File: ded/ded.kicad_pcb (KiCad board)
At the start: 2 copper layers, 10.6 x 15 mm, 2 parts, among them J1 USB_C_Receptacle_PowerOnly_6P, J2 USB_C_Receptacle_PowerOnly_6P

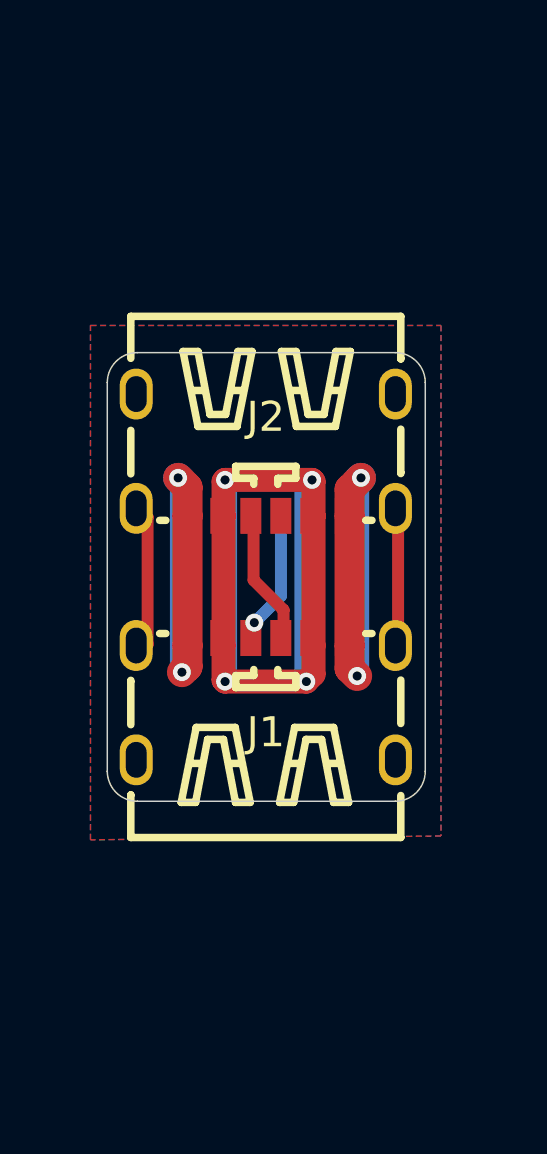
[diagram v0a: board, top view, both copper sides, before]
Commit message: add a hopefully-more-bendable spot to the usb coupler; fix drc; add sds
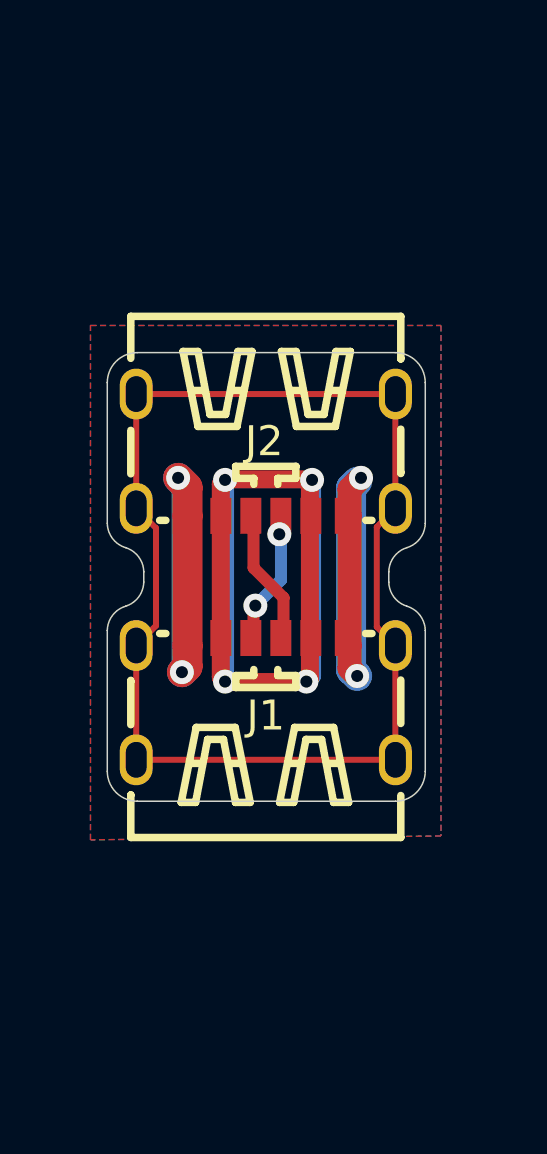
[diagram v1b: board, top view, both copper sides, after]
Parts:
- added G***: LOGO, ded:sds5050, B.Cu at (100.0, 101.1)
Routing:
- net /S1: track 0.00 -> 42.7 mm
- net (no net): track 9.88 -> 0.00 mm
- net Net-(J1-CC1): track 4.83 -> 4.75 mm, vias 1 -> 2
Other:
- outline, holes or cut-outs redrawn

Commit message: candidate designs for ded and deh couplers
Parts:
- removed J1, J2: USB_C_Receptacle_PowerOnly_6P, ded:TYPE-C-SMD_TYPE-C-6P_5
- added USB1: GT-USB-8016A, ded:USB-TYPE-C-SMD_GT-USB-8016A, F.Cu at (100.0, 106.3)
- added USB2: GT-USB-8016A, ded:USB-TYPE-C-SMD_GT-USB-8016A, F.Cu at (100.0, 95.9)
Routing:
- net /S1: track 42.7 -> 0.00 mm
- net VBUS: track 32.8 -> 9.93 mm, vias 4 -> 0
- net GND: track 26.9 -> 8.32 mm, vias 4 -> 3
- net Net-(USB1-TX1+): track 0.00 -> 13.2 mm, vias 0 -> 2
- net Net-(USB1-TX1-): track 0.00 -> 13.0 mm, vias 0 -> 2
- net Net-(USB1-RX1-): track 0.00 -> 12.0 mm, vias 0 -> 2
- net Net-(USB1-CC1): track 0.00 -> 11.2 mm, vias 0 -> 2
- net Net-(USB1-RX1+): track 0.00 -> 11.2 mm, vias 0 -> 2
- net Net-(USB1-D+): track 0.00 -> 10.0 mm, vias 0 -> 2
- net Net-(USB1-D-): track 0.00 -> 9.96 mm, vias 0 -> 2
- net (no net): track 0.00 -> 8.71 mm
- net Net-(J1-CC1): track 4.75 -> 0.00 mm, vias 2 -> 0
- net Net-(J1-CC2): track 4.74 -> 0.00 mm
- added copper zone on B.Cu, net GND
- added copper zone on F.Cu, net VBUS
- removed copper zone on F.Cu, net GND
- removed copper zone on B.Cu, net VBUS
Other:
- board size 10.6 x 15 mm -> 13 x 15.2 mm

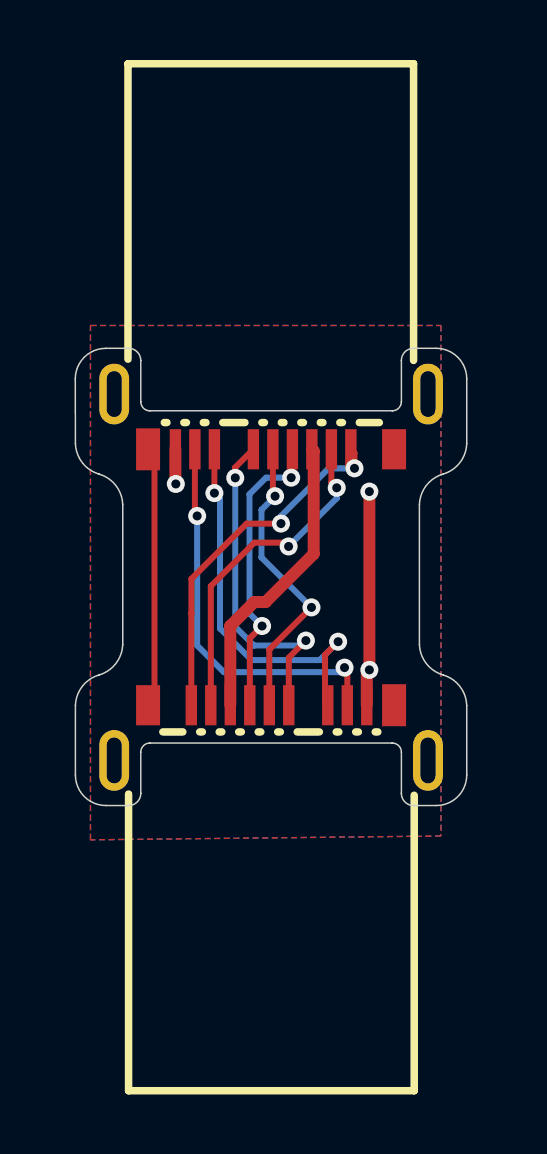
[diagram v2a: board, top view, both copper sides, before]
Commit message: layout on ded to make it a little shorter and give the thts a little more space
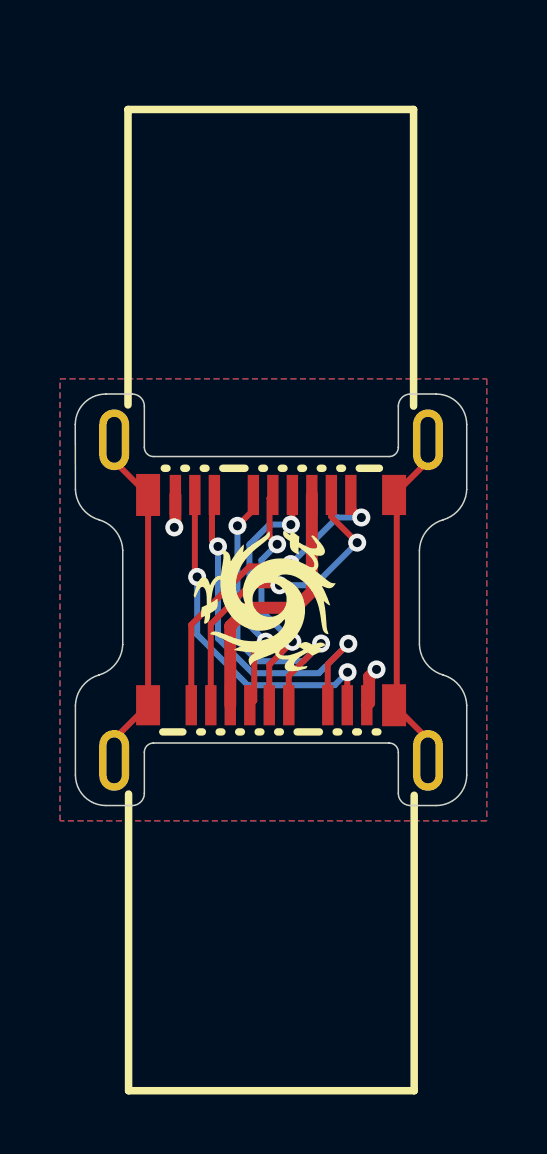
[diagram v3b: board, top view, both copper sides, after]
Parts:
- G***: moved to F.Cu
- moved USB2 1.52 mm to (100.0, 97.4)
- moved G*** 0.76 mm to (99.9, 101.9), turned to 0 degrees
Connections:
- USB1 pad S1: (no net) -> Net-(USB1-Shield)
- USB2 pad S1: (no net) -> Net-(USB1-Shield)
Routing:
- net Net-(USB1-Shield): track 0.00 -> 23.3 mm
- net (no net): track 8.71 -> 0.00 mm
- net GND: track 8.32 -> 2.42 mm, vias 3 -> 2
- net Net-(USB1-D+): track 10.0 -> 8.12 mm
- net Net-(USB1-TX1+): track 13.2 -> 11.7 mm
- net Net-(USB1-D-): track 9.96 -> 8.47 mm
- net Net-(USB1-RX1-): track 12.0 -> 10.7 mm
- net VBUS: track 9.93 -> 9.06 mm
- net Net-(USB1-TX1-): track 13.0 -> 12.5 mm
- net Net-(USB1-RX1+): track 11.2 -> 10.7 mm
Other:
- board size 13 x 15.2 mm -> 13 x 13.7 mm

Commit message: ded: add stiffener layer
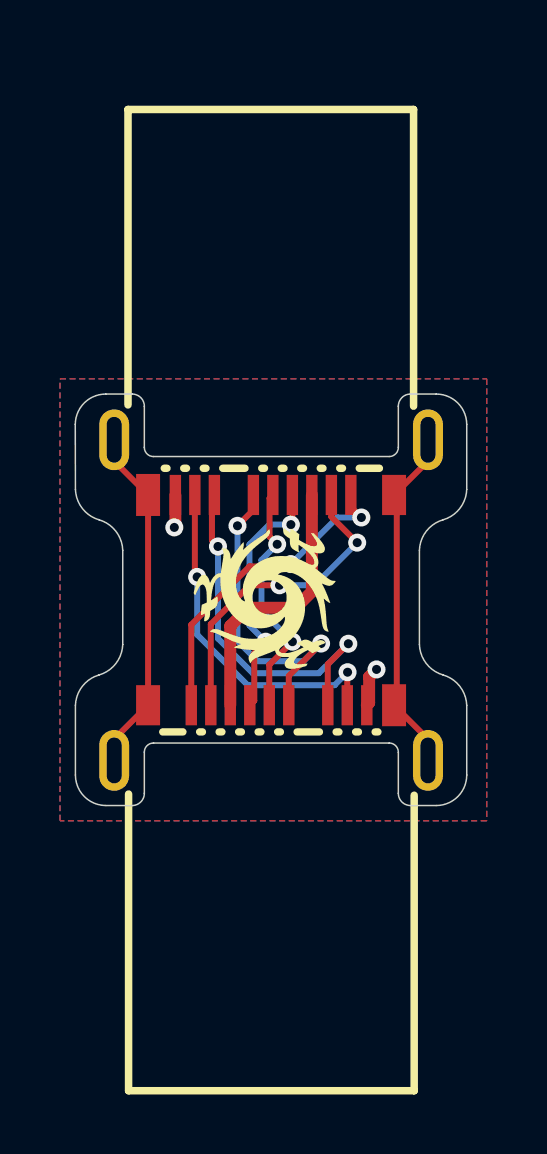
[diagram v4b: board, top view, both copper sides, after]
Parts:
- added G***: LOGO, ded:sds5050, B.Cu at (100.0, 101.8)
- moved G*** 0.08 mm to (99.9, 101.8)
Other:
- board text added: "Stiffener: Stainless Steel Location: Stiffener layer (back side) Thickness: 0.2mm"
